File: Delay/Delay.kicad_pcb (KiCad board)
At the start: 2 copper layers, 192.7 x 104.5 mm, 186 parts, among them J101 Conn_02x08_Odd_Even, J102 AudioJack2_SwitchT, J103 AudioJack2_SwitchT, J104 AudioJack2_SwitchT, J105 AudioJack2_SwitchT, J106 AudioJack2_SwitchT, J107 AudioJack2_SwitchT, J108 AudioJack2_SwitchT, J201 AudioJack2_SwitchT, J301 AudioJack2_SwitchT, J401 AudioJack2_SwitchT, Q201 2N3904, Q301 2N3904, Q401 2N3904, SW101 SW_SPDT, SW102 SW_SPDT, U201 TL072, U202 TL072, U203 TL072, U204 PT2399, U301 TL072, U302 TL072, U303 TL072, U304 PT2399, U401 TL072, U402 TL072, U403 TL072, U404 PT2399

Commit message: Begin revised delay
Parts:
- removed C107, C108, C109, C215, C216, C315, C316, C415, C416: 10u, Capacitor_THT:C_Disc_D5.0mm_W2.5mm_P5.00mm
- removed C201, C203, C206, C210, C211, C217, C218, C219, C220, C221, C222, C301, C303, C306, C310, C311, C317, C318, C319, C320, C321, C322, C401, C403, C406, C410, C411, C417, C418, C419, C420, C421, C422: 0.1u, Capacitor_THT:C_Disc_D5.0mm_W2.5mm_P5.00mm
- removed C202, C302, C402: 100u, Capacitor_THT:CP_Radial_D5.0mm_P2.00mm
- removed C204, C208, C304, C308, C404, C408: 4.7u, Capacitor_THT:C_Disc_D5.0mm_W2.5mm_P5.00mm
- removed C205, C305, C405: 47u, Capacitor_THT:CP_Radial_D5.0mm_P2.00mm
- removed C207, C214, C307, C314, C407, C414: 4.7n, Capacitor_THT:C_Disc_D5.0mm_W2.5mm_P5.00mm
- removed C209, C212, C309, C312, C409, C412: 680p, Capacitor_THT:C_Disc_D5.0mm_W2.5mm_P5.00mm
- removed C213, C313, C413: 10n, Capacitor_THT:C_Disc_D5.0mm_W2.5mm_P5.00mm
- removed D101, D102, D103: 1N5819, Diode_THT:D_DO-41_SOD81_P10.16mm_Horizontal
- removed D201, D301, D401: 1N4148, Diode_THT:D_DO-35_SOD27_P7.62mm_Horizontal
- removed J101: Conn_02x08_Odd_Even, Connector_PinHeader_2.54mm:PinHeader_2x08_P2.54mm_Vertical
- removed J102, J103, J104, J105, J106, J107, J108, J201, J301, J401: AudioJack2_SwitchT, Connector_Audio:Jack_3.5mm_QingPu_WQP-PJ398SM_Vertical_CircularHoles
- removed Q201, Q301, Q401: 2N3904, Package_TO_SOT_THT:TO-92_HandSolder
- removed R101, R102, R103: 10, Resistor_THT:R_Axial_DIN0207_L6.3mm_D2.5mm_P7.62mm_Horizontal
- removed R201, R206, R212, R301, R306, R312, R401, R406, R412: 100k, Resistor_THT:R_Axial_DIN0207_L6.3mm_D2.5mm_P7.62mm_Horizontal
- removed R202, R203, R204, R205, R208, R302, R303, R304, R305, R308, R402, R403, R404, R405, R408: 150k, Resistor_THT:R_Axial_DIN0207_L6.3mm_D2.5mm_P7.62mm_Horizontal
- removed R207, R217, R222, R307, R317, R322, R407, R417, R422: 5.6k, Resistor_THT:R_Axial_DIN0207_L6.3mm_D2.5mm_P7.62mm_Horizontal
- removed R209, R213, R218, R309, R313, R318, R409, R413, R418: 15k, Resistor_THT:R_Axial_DIN0207_L6.3mm_D2.5mm_P7.62mm_Horizontal
- removed R210, R221, R310, R321, R410, R421: 1.5k, Resistor_THT:R_Axial_DIN0207_L6.3mm_D2.5mm_P7.62mm_Horizontal
- removed R211, R223, R311, R323, R411, R423: 1k, Resistor_THT:R_Axial_DIN0207_L6.3mm_D2.5mm_P7.62mm_Horizontal
- removed R214, R314, R414: 8.2k, Resistor_THT:R_Axial_DIN0207_L6.3mm_D2.5mm_P7.62mm_Horizontal
- removed R215, R216, R219, R220, R315, R316, R319, R320, R415, R416, R419, R420: 10k, Resistor_THT:R_Axial_DIN0207_L6.3mm_D2.5mm_P7.62mm_Horizontal
- removed RV101, RV102, RV201, RV202, RV203, RV301, RV302, RV303, RV401, RV402, RV403: 50k, Potentiometer_THT:Potentiometer_Alpha_RD901F-40-00D_Single_Vertical_CircularHoles
- removed SW101, SW102: SW_SPDT, Custom:MTS-102_MTS-103_MTS-112_MTS-113_MTS-123
- removed U201, U202, U203, U301, U302, U303, U401, U402, U403: TL072, Package_DIP:DIP-8_W7.62mm_Socket
- removed U204, U304, U404: PT2399, Package_DIP:DIP-16_W7.62mm_Socket
- added C1: 10u, 0_Capacitor_THT:C_Disc_D5.5mm_W4.0mm_P2.50mm, B.Cu at (143.4, 72.4)
- added C10: 0.22u, 0_Capacitor_THT:C_Disc_D5.5mm_W2.5mm_P2.50mm, B.Cu at (141.1, 37.7)
- added C11: 0.1u, 0_Capacitor_THT:C_Disc_D5.5mm_W2.5mm_P2.50mm, B.Cu at (162.8, 68.3)
- added C12: 0.1u, 0_Capacitor_THT:C_Disc_D5.5mm_W2.5mm_P2.50mm, B.Cu at (150.8, 111.7)
- added C13: 0.1u, 0_Capacitor_THT:C_Disc_D5.5mm_W2.5mm_P2.50mm, B.Cu at (164.4, 122.6)
- added C14: 4.7n, 0_Capacitor_THT:C_Disc_D5.5mm_W2.5mm_P2.50mm, B.Cu at (157.0, 109.1)
- added C15: 4.7u, Capacitor_THT:C_Disc_D3.8mm_W2.6mm_P2.50mm, B.Cu at (147.8, 106.2)
- added C16: 0.1u, 0_Capacitor_THT:C_Disc_D5.5mm_W2.5mm_P2.50mm, B.Cu at (141.1, 32.6)
- added C17: 680p, 0_Capacitor_THT:C_Disc_D5.5mm_W2.5mm_P2.50mm, B.Cu at (149.3, 48.4)
- added C18: 0.1u, 0_Capacitor_THT:C_Disc_D5.5mm_W2.5mm_P2.50mm, B.Cu at (149.3, 60.8)
- added C19: 0.1u, 0_Capacitor_THT:C_Disc_D5.5mm_W2.5mm_P2.50mm, B.Cu at (149.3, 67.0)
- added C2: 10u, 0_Capacitor_THT:C_Disc_D5.5mm_W4.0mm_P2.50mm, B.Cu at (140.8, 100.6)
- added C20: 680p, 0_Capacitor_THT:C_Disc_D5.5mm_W2.5mm_P2.50mm, B.Cu at (149.3, 54.6)
- added C21: 10n, 0_Capacitor_THT:C_Disc_D5.5mm_W2.5mm_P2.50mm, B.Cu at (137.2, 64.1)
- added C22: 4.7n, 0_Capacitor_THT:C_Disc_D5.5mm_W2.5mm_P2.50mm, B.Cu at (134.5, 54.5)
- added C23: 10u, 0_Capacitor_THT:C_Disc_D5.5mm_W4.0mm_P2.50mm, B.Cu at (137.2, 71.3)
- added C24: 10u, 0_Capacitor_THT:C_Disc_D5.5mm_W4.0mm_P2.50mm, B.Cu at (144.2, 50.6)
- added C25: 10p, 0_Capacitor_THT:C_Disc_D5.5mm_W2.5mm_P2.50mm, B.Cu at (147.6, 117.6)
- added C3: 0.1u, 0_Capacitor_THT:C_Disc_D5.5mm_W2.5mm_P2.50mm, B.Cu at (158.5, 46.9)
- added C4: 100u, Capacitor_THT:CP_Radial_D6.3mm_P2.50mm, B.Cu at (162.8, 46.7)
- added C5: 0.1u, 0_Capacitor_THT:C_Disc_D5.5mm_W2.5mm_P2.50mm, B.Cu at (168.5, 83.8)
- added C6: 0.1u, 0_Capacitor_THT:C_Disc_D5.5mm_W2.5mm_P2.50mm, B.Cu at (154.3, 88.8)
- added C7: 0.1u, 0_Capacitor_THT:C_Disc_D5.5mm_W2.5mm_P2.50mm, B.Cu at (162.8, 65.2)
- added C8: 4.7u, Capacitor_THT:C_Disc_D3.8mm_W2.6mm_P2.50mm, B.Cu at (165.4, 109.1)
- added C9: 47u, Capacitor_THT:CP_Radial_D5.0mm_P2.50mm, B.Cu at (163.9, 52.8)
- added D1: 1N5819, Diode_THT:D_DO-41_SOD81_P10.16mm_Horizontal, B.Cu at (150.0, 74.8)
- added D2: 1N5819, Diode_THT:D_DO-41_SOD81_P10.16mm_Horizontal, B.Cu at (150.0, 87.9)
- added D3: 1N4148, Diode_THT:D_DO-35_SOD27_P7.62mm_Horizontal, B.Cu at (157.5, 74.4)
- added D4: 1N5819, Diode_THT:D_DO-41_SOD81_P10.16mm_Horizontal, B.Cu at (134.9, 40.3)
- added D5: 1N5819, Diode_THT:D_DO-41_SOD81_P10.16mm_Horizontal, B.Cu at (131.4, 30.1)
- added H1: MNT_STANDOFF, 0_MountingHole:MountingHole_Pitch7.5mm_Drill3.4mm, F.Cu at (165.4, 27.2)
- added H2: MNT_STANDOFF, 0_MountingHole:MountingHole_Pitch7.5mm_Drill3.4mm, F.Cu at (126.9, 119.7)
- added J1: Conn_02x05_Top_Bottom, Connector_Molex:Molex_Mini-Fit_Jr_5566-10A_2x05_P4.20mm_Vertical, B.Cu at (137.9, 78.1)
- added J2: Conn_01x14_Pin, Connector_PinHeader_2.54mm:PinHeader_1x14_P2.54mm_Vertical, F.Cu at (130.9, 66.2)
- added Q1: 2N3904, Package_TO_SOT_THT:TO-92_HandSolder, B.Cu at (165.1, 61.4)
- added R1: 100k, Resistor_THT:R_Axial_DIN0207_L6.3mm_D2.5mm_P7.62mm_Horizontal, B.Cu at (157.7, 97.9)
- added R10: 8.2k, Resistor_THT:R_Axial_DIN0207_L6.3mm_D2.5mm_P7.62mm_Horizontal, B.Cu at (145.0, 105.9)
- added R11: 10k, Resistor_THT:R_Axial_DIN0207_L6.3mm_D2.5mm_P7.62mm_Horizontal, B.Cu at (145.0, 109.1)
- added R12: 10k, Resistor_THT:R_Axial_DIN0207_L6.3mm_D2.5mm_P7.62mm_Horizontal, B.Cu at (145.0, 112.3)
- added R13: 5.6k, Resistor_THT:R_Axial_DIN0207_L6.3mm_D2.5mm_P7.62mm_Horizontal, B.Cu at (144.8, 67.3)
- added R14: 15k, Resistor_THT:R_Axial_DIN0207_L6.3mm_D2.5mm_P7.62mm_Horizontal, B.Cu at (144.8, 54.5)
- added R15: 10k, Resistor_THT:R_Axial_DIN0207_L6.3mm_D2.5mm_P7.62mm_Horizontal, B.Cu at (144.8, 57.7)
- added R16: 10k, Resistor_THT:R_Axial_DIN0207_L6.3mm_D2.5mm_P7.62mm_Horizontal, B.Cu at (144.8, 60.9)
- added R17: 1.5k, Resistor_THT:R_Axial_DIN0207_L6.3mm_D2.5mm_P7.62mm_Horizontal, B.Cu at (144.4, 115.0)
- added R18: 5.6k, Resistor_THT:R_Axial_DIN0207_L6.3mm_D2.5mm_P7.62mm_Horizontal, B.Cu at (138.0, 115.0)
- added R19: 1k, Resistor_THT:R_Axial_DIN0207_L6.3mm_D2.5mm_P7.62mm_Horizontal, B.Cu at (141.2, 115.0)
- added R2: 100k, Resistor_THT:R_Axial_DIN0207_L6.3mm_D2.5mm_P7.62mm_Horizontal, B.Cu at (165.1, 80.5)
- added R3: 5.6k, Resistor_THT:R_Axial_DIN0207_L6.3mm_D2.5mm_P7.62mm_Horizontal, B.Cu at (168.1, 112.2)
- added R4: 150k, Resistor_THT:R_Axial_DIN0207_L6.3mm_D2.5mm_P7.62mm_Horizontal, B.Cu at (157.5, 77.3)
- added R5: 15k, Resistor_THT:R_Axial_DIN0207_L6.3mm_D2.5mm_P7.62mm_Horizontal, B.Cu at (165.3, 94.7)
- added R6: 1.5k, Resistor_THT:R_Axial_DIN0207_L6.3mm_D2.5mm_P7.62mm_Horizontal, B.Cu at (164.9, 119.8)
- added R7: 1k, Resistor_THT:R_Axial_DIN0207_L6.3mm_D2.5mm_P7.62mm_Horizontal, B.Cu at (168.4, 62.3)
- added R8: 100k, Resistor_THT:R_Axial_DIN0207_L6.3mm_D2.5mm_P7.62mm_Horizontal, B.Cu at (161.7, 112.2)
- added R9: 15k, Resistor_THT:R_Axial_DIN0207_L6.3mm_D2.5mm_P7.62mm_Horizontal, B.Cu at (164.7, 105.7)
- added U1: TL072, Package_DIP:DIP-8_W7.62mm_Socket, B.Cu at (165.2, 91.4)
- added U2: TL072, Package_DIP:DIP-8_W7.62mm_Socket, B.Cu at (158.4, 115.0)
- added U3: PT2399, Package_DIP:DIP-16_W7.62mm, B.Cu at (159.7, 50.1)
- added U4: LM7805_TO220, Package_TO_SOT_THT:TO-220-3_Vertical, B.Cu at (145.2, 37.7)
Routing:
- net +12V: track 513.4 -> 148.6 mm, vias 29 -> 0
- net /Delay1/MasterTimeCV: track 323.3 -> 0.00 mm, vias 8 -> 0
- net -12V: track 363.9 -> 80.1 mm, vias 25 -> 0
- net /Delay1/MasterTime: track 255.0 -> 0.00 mm
- net +5V: track 205.9 -> 39.2 mm, vias 12 -> 0
- net Net-(C415-Pad2): track 91.7 -> 0.00 mm, vias 2 -> 0
- net Net-(C315-Pad2): track 91.7 -> 0.00 mm, vias 2 -> 0
- net Net-(C215-Pad2): track 91.7 -> 0.00 mm, vias 2 -> 0
- net Net-(R414-Pad2): track 72.8 -> 0.00 mm
- net Net-(R314-Pad2): track 72.8 -> 0.00 mm
- net Net-(R214-Pad2): track 72.8 -> 0.00 mm
- net Net-(C209-Pad2): track 69.3 -> 0.00 mm
- net Net-(C409-Pad2): track 69.3 -> 0.00 mm
- net Net-(C309-Pad2): track 69.3 -> 0.00 mm
- net Net-(C212-Pad1): track 61.5 -> 0.00 mm
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- added copper zone on F.Cu, net GND
- removed copper zone on B.Cu, net GND
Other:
- board size 192.7 x 104.5 mm -> 50.5 x 104.5 mm

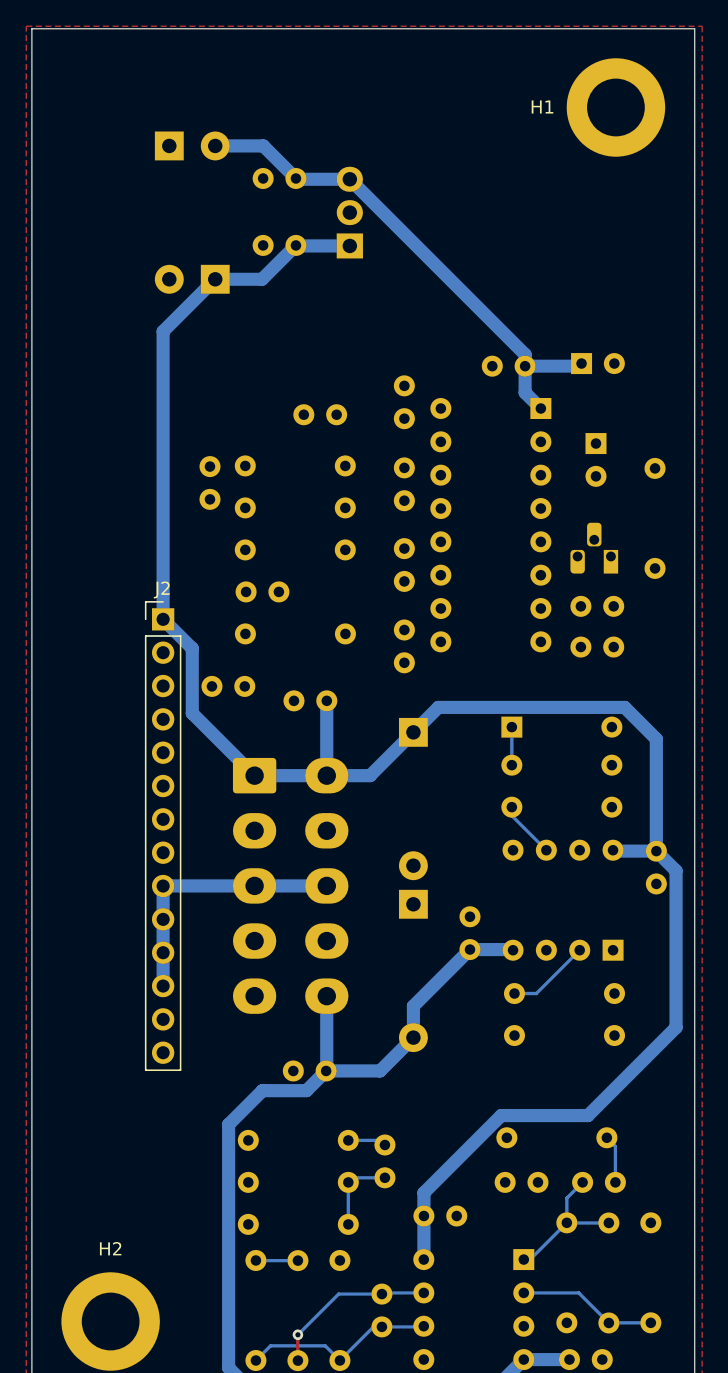
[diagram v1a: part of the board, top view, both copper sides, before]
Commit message: Finish diode ladder filter
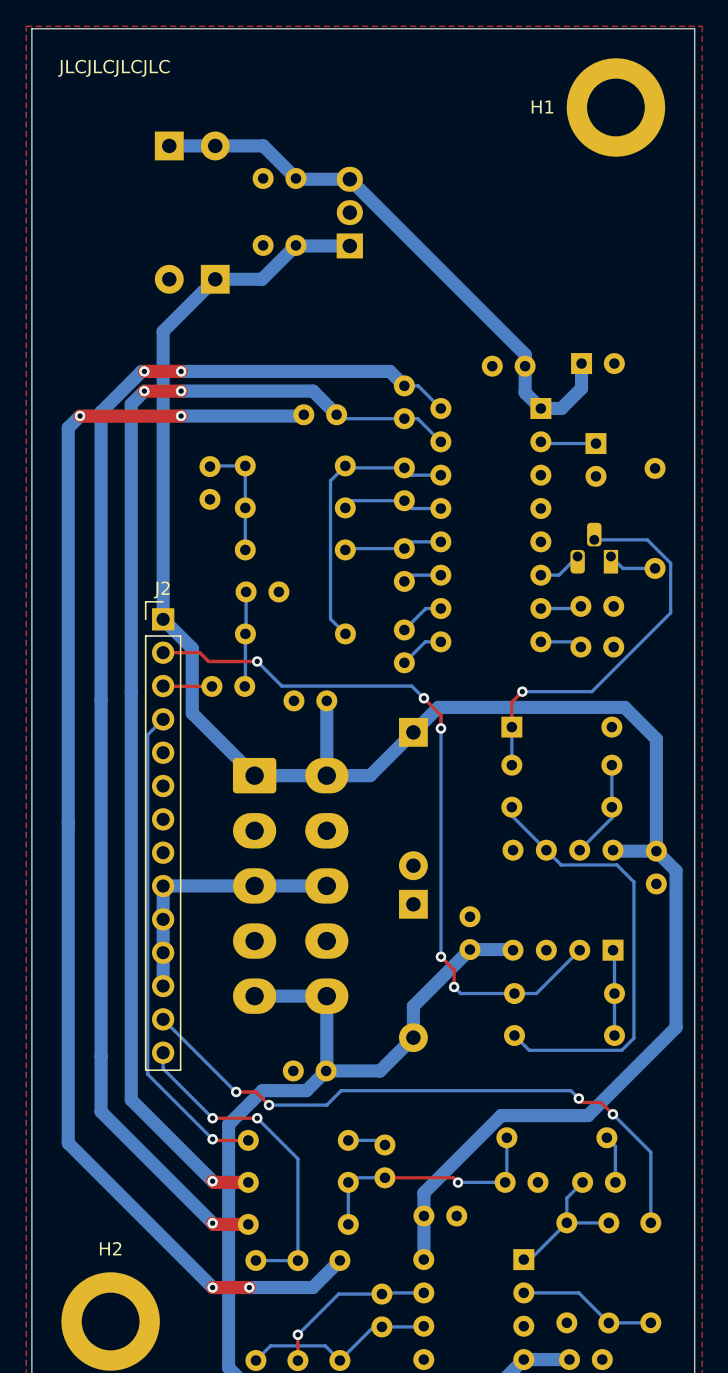
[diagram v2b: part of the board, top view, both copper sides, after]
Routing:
- net Net-(C24-Pad2): track 0.00 -> 99.0 mm, vias 0 -> 4
- net Net-(U3-LPF1-IN): track 0.00 -> 96.4 mm, vias 0 -> 3
- net Net-(U3-LPF1-OUT): track 0.00 -> 90.1 mm, vias 0 -> 3
- net /TIME: track 6.34 -> 55.4 mm, vias 0 -> 5
- net /IN: track 0.00 -> 47.6 mm, vias 0 -> 4
- net /FB_2: track 0.00 -> 37.3 mm, vias 0 -> 1
- net Net-(U1B--): track 4.37 -> 33.9 mm
- net Net-(D3-K): track 2.90 -> 30.1 mm, vias 0 -> 1
- net /OUT: track 3.20 -> 25.3 mm, vias 0 -> 2
- net Net-(U3-LPF2-OUT): track 0.00 -> 21.3 mm
- net Net-(C14-Pad1): track 6.13 -> 18.9 mm, vias 0 -> 1
- net Net-(C22-Pad1): track 0.00 -> 9.11 mm
- net Net-(U3-LPF2-IN): track 0.00 -> 7.75 mm
- net Net-(U3-OP2-OUT): track 0.00 -> 7.53 mm
- net Net-(R2-Pad1): track 0.00 -> 7.49 mm
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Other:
- board text added: "Delay V1 Matthew Taylor"
- board text added: "JLCJLCJLCJLC"
